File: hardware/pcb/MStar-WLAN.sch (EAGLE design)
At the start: 39 parts, among them J1 6P6C, J3 ZX62R-B-5P(30), Q1 VP2106, Q2 2N3904

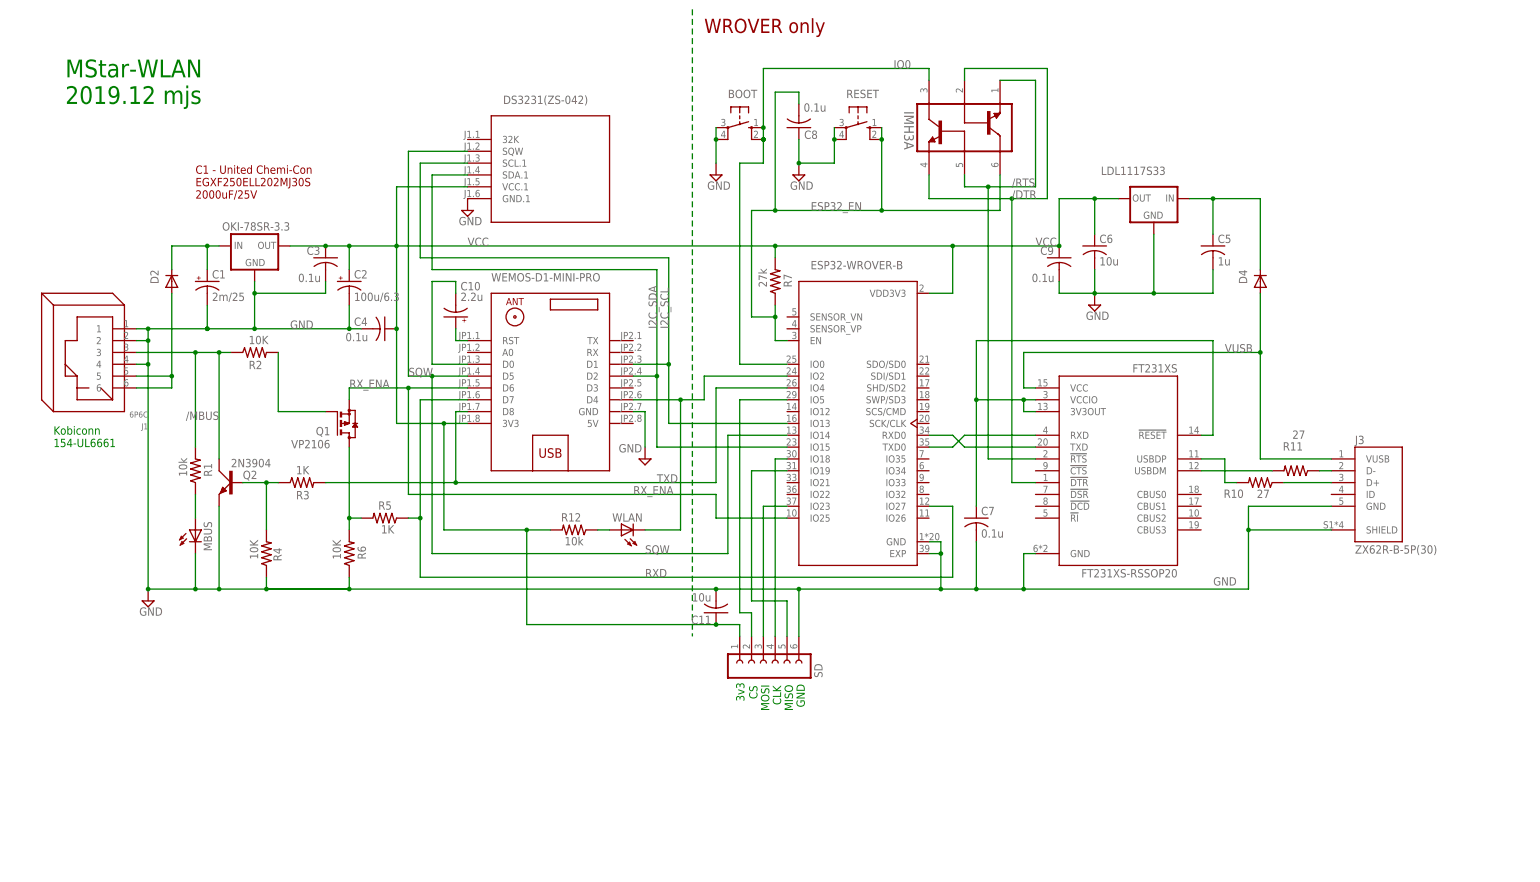
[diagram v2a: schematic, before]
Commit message: bug fixes. SD Card support. New PCB.
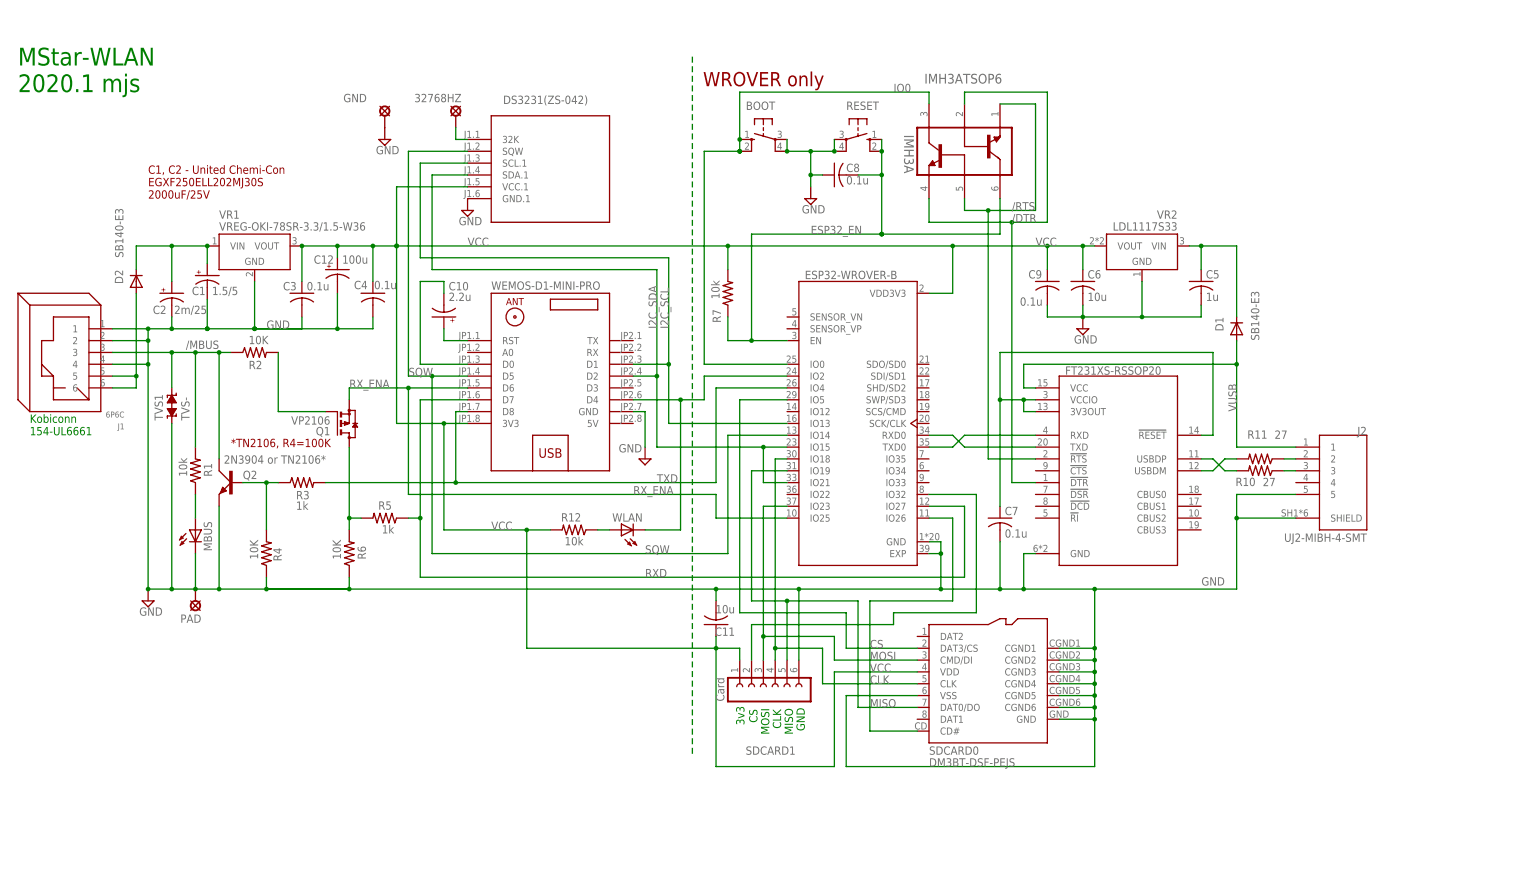
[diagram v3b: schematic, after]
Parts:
- removed D4: (no value), diode:DIODE-D-5
- removed J3: ZX62R-B-5P(30), MyLibrary:ZX62R-B-5P(30)
- removed LDL1117S33: LM1117MP-3.3, MyLibrary:LM1117MP-3.3
- removed OKI-78SR-3.3: (no value), v-reg:78MXXS
- removed SD: (no value), con-lsta:FE06-1
- added 32768HZ, GND: MCS10B, MStar-WLAN:MCS10B
- added C12: 100u, MStar-WLAN:CPOL-USE2.5-6
- added D1: SB140-E3, MStar-WLAN:DIODE-
- added J2: UJ2-MIBH-4-SMT, MStar-WLAN:UJ2-MIBH-4-SMT
- added PAD: LSP10, MStar-WLAN:LSP10
- added SDCARD0: DM3BT-DSF-PEJS, MStar-WLAN:DM3BT-DSF-PEJS
- added SDCARD1: Card, MStar-WLAN:FE06-1
- added TVS1: TVS-, MStar-WLAN:TVS-
- added VR1: VREG-OKI-78SR-3.3/1.5-W36, MStar-WLAN:VREG-OKI-78SR-3.3/1.5-W36
- added VR2: LDL1117S33, MStar-WLAN:VREG-TS1117CW-3V3
- BOOT, RESET: device switch-omron:10-XX -> MStar-WLAN:10-XX
- C1: value 2m/25 -> 1.5/5; device rcl:CPOL-USE5-10.5 -> MStar-WLAN:CPOL-USE5-4
- C10: device rcl:CPOL-USE2.5-5 -> MStar-WLAN:CPOL-USE2.5-5
- C11, C5, C6: device rcl:C-USC1206 -> MStar-WLAN:C-USC1206
- C2: value 100u/6.3 -> 2m/25; device rcl:CPOL-USE2.5-6 -> MStar-WLAN:CPOL-USE5-4
- C3, C4, C7, C8, C9: device rcl:C-US025-024X044 -> MStar-WLAN:C-US025-024X044
- D2: value (none) -> SB140-E3; device diode:DIODE-D-5 -> MStar-WLAN:DIODE-DO41-7.6
- DS3231(ZS-042): device MyLibrary:RTC-DS3231-AT24C32-6 -> MStar-WLAN:RTC-DS3231-AT24C32-6
- ESP32-WROVER-B: device MyLibrary:ESP32-WROVER-I -> MStar-WLAN:ESP32-WROVER-I
- FT231XS: device MyLibrary:FT231XS-RSSOP20 -> MStar-WLAN:FT231XS-RSSOP20
- IMH3A: device MyLibrary:IMH3ATSOP6 -> MStar-WLAN:IMH3ATSOP6
- J1: device con-rj:RJ12 -> MStar-WLAN:RJ12
- MBUS, WLAN: device adafruit:LED3MM -> MStar-WLAN:LED3MM
- Q1: device MyLibrary:VP2106 -> MStar-WLAN:VP2106
- Q2: value 2N3904 -> 2N3904 or TN2106*; device transistor-small-signal:2N3904 -> MStar-WLAN:2N3904"
- R1, R10, R11, R12, R2, R4, R6: device rcl:R-US_0207/2V -> MStar-WLAN:R-US_
- R3, R5: value 1K -> 1k; device rcl:R-US_0207/2V -> MStar-WLAN:R-US_
- R7: value 27k -> 10k; device rcl:R-US_0207/2V -> MStar-WLAN:R-US_
- U$1: device MyLibrary:WEMOS-D1-MINI-PRO -> MStar-WLAN:WEMOS-D1-MINI-PRO
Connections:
- net N$19 renamed WLAN_LED
- net N$4 renamed WEMOS_RST
- net N$5 renamed TXD0
- net N$6 renamed RXD0
- net N$7 renamed SELF_RESET
- removed net N$16: ESP32-WROVER-B.IO5, SD.2
- removed net N$20: ESP32-WROVER-B.IO18, SD.4
- removed net N$22: ESP32-WROVER-B.IO23, SD.3
- removed net N$8: ESP32-WROVER-B.IO19, SD.5
- new net CLK: ESP32-WROVER-B.IO18, SDCARD0.CLK, SDCARD1.4
- new net CS: ESP32-WROVER-B.IO5, SDCARD0.DAT3/CS
- new net MISO: ESP32-WROVER-B.IO19, SDCARD0.DAT0/DO, SDCARD1.5
- new net MOSI: ESP32-WROVER-B.IO23, SDCARD0.CMD/DI, SDCARD1.3
- new net N$4: ESP32-WROVER-B.IO26, SDCARD0.CD#
- new net N$5: 32768HZ.MP, DS3231(ZS-042).32K
- new net N$7: ESP32-WROVER-B.IO32, SDCARD1.2
- net /MBUS: now also TVS1.2
- net GND: now also C12.-, GND.MP, J2.5, J2.SHIELD, PAD.MP, SDCARD0.CGND1, SDCARD0.CGND2, SDCARD0.CGND3, SDCARD0.CGND4, SDCARD0.CGND5, SDCARD0.CGND6, SDCARD0.GND, SDCARD0.VSS, SDCARD1.6, TVS1.1, VR1.GND, VR2.GND; no longer J3.GND, J3.SHIELD, LDL1117S33.GND, OKI-78SR-3.3.GND, SD.6
- net I2C_SDA: now also ESP32-WROVER-B.IO21
- net N$10: now also J2.2; no longer J3.D-
- net N$17: now also D1.C, VR2.VIN; no longer D4.C, LDL1117S33.IN
- net N$9: now also J2.3; no longer J3.D+
- net RAW12: now also C2.+, VR1.VIN; no longer OKI-78SR-3.3.IN
- net VCC: now also C12.+, SDCARD0.VDD, SDCARD1.1, VR1.VOUT, VR2.VOUT; no longer C2.+, LDL1117S33.OUT, OKI-78SR-3.3.OUT, SD.1
- net VUSB: now also D1.A, J2.1; no longer D4.A, J3.VUSB
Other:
- note added: "*TN2106, R4=100K"
- note added: "C1, C2 - United Chemi-Con EGXF250ELL202MJ30S 2000uF/25V"
- note added: "MStar-WLAN 2020.1 mjs"
- note removed: "C1 - United Chemi-Con EGXF250ELL202MJ30S 2000uF/25V"
- note removed: "MStar-WLAN 2019.12 mjs"
- moved on the sheet: BOOT, D2, IMH3A, J1, R10, R11, R7, RESET

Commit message: ESP32. Logging. Dynamic status update. More.
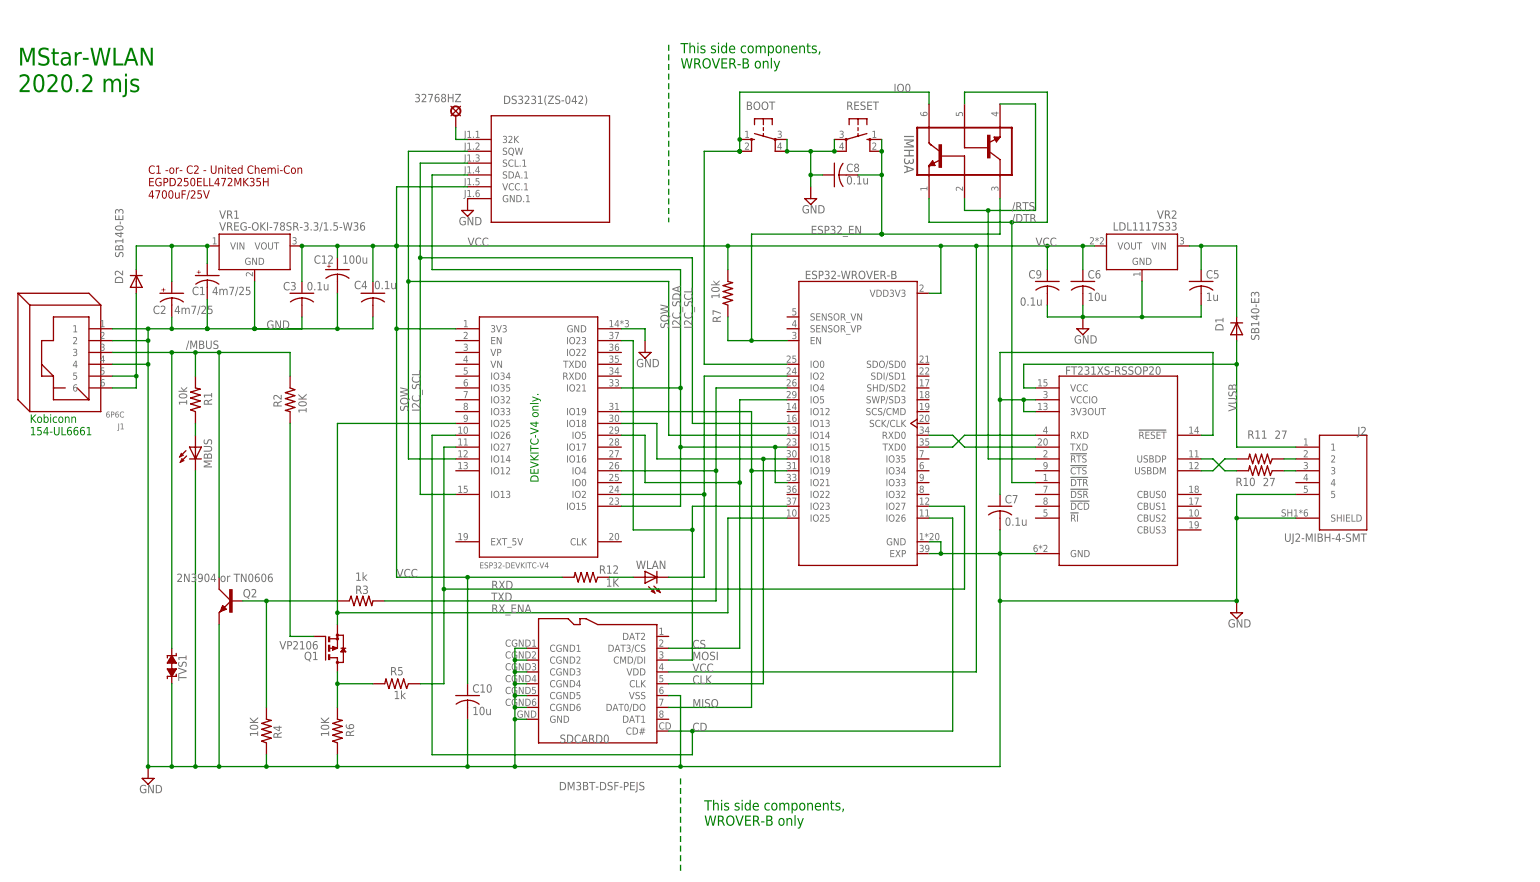
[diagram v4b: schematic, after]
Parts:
- removed C11: 10u, MStar-WLAN:C-USC1206
- removed GND: MCS10B, MStar-WLAN:MCS10B
- removed PAD: LSP10, MStar-WLAN:LSP10
- removed SDCARD1: Card, MStar-WLAN:FE06-1
- C1: value 1.5/5 -> 4m7/25
- C10: value 2.2u -> 10u; device MStar-WLAN:CPOL-USE2.5-5 -> MStar-WLAN:C-USC1206
- C2: value 2m/25 -> 4m7/25
- Q2: value 2N3904 or TN2106* -> 2N3904 or TN0606
- R12: value 10k -> 1K
- U$1: value WEMOS-D1-MINI-PRO -> ESP32-DEVKITC-V4-NOSD; device MStar-WLAN:WEMOS-D1-MINI-PRO -> MStar-WLAN:ESP32-DEVKITC-V4-NOSD
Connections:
- removed net N$4: ESP32-WROVER-B.IO26, SDCARD0.CD#
- removed net N$7: ESP32-WROVER-B.IO32, SDCARD1.2
- removed net SELF_RESET: C10.-, U$1.D0
- removed net WEMOS_RST: C10.+, U$1.RST
- new net CD: ESP32-WROVER-B.IO26, SDCARD0.CD#, U$1.IO26
- net /DTR: now also IMH3A.Q1E, IMH3A.Q2B; no longer IMH3A.Q1B, IMH3A.Q2E
- net /RTS: now also IMH3A.Q1B, IMH3A.Q2E; no longer IMH3A.Q1E, IMH3A.Q2B
- net CLK: now also U$1.IO18; no longer SDCARD1.4
- net CS: now also U$1.IO5
- net ESP32_EN: now also IMH3A.Q2C; no longer IMH3A.Q1C
- net GND: now also C10.2; no longer C11.2, GND.MP, PAD.MP, SDCARD1.6
- net I2C_SCL: now also U$1.IO13; no longer U$1.D1
- net I2C_SDA: now also U$1.IO15, U$1.IO21; no longer U$1.D2
- net IO0: now also IMH3A.Q1C; no longer IMH3A.Q2C
- net MISO: now also U$1.IO19; no longer SDCARD1.5
- net MOSI: now also U$1.IO23; no longer SDCARD1.3
- net RXD: now also U$1.IO27; no longer U$1.D7
- net RX_ENA: now also U$1.IO25; no longer U$1.D6
- net SQW: now also U$1.IO14; no longer U$1.D5
- net TXD: now also U$1.IO4; no longer U$1.D8
- net VCC: now also C10.1; no longer C11.1, SDCARD1.1
- net WLAN_LED: now also U$1.IO2; no longer U$1.D4
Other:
- note added: "C1 -or- C2 - United Chemi-Con EGPD250ELL472MK35H 4700uF/25V"
- note added: "DEVKITC-V4 only."
- note added: "MStar-WLAN 2020.2 mjs"
- note added: "This side components, WROVER-B only"
- note removed: "*TN2106, R4=100K"
- note removed: "3v3"
- note removed: "C1, C2 - United Chemi-Con EGXF250ELL202MJ30S 2000uF/25V"
- note removed: "CLK"
- note removed: "CS"
- note removed: "GND"
- note removed: "MISO"
- note removed: "MOSI"
- note removed: "MStar-WLAN 2020.1 mjs"
- note removed: "WROVER only"
- moved on the sheet: C7, IMH3A, MBUS, Q1, Q2, R1, R12, R2, R3, R4, R5, R6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

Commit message: Logging, hardware change to USB C
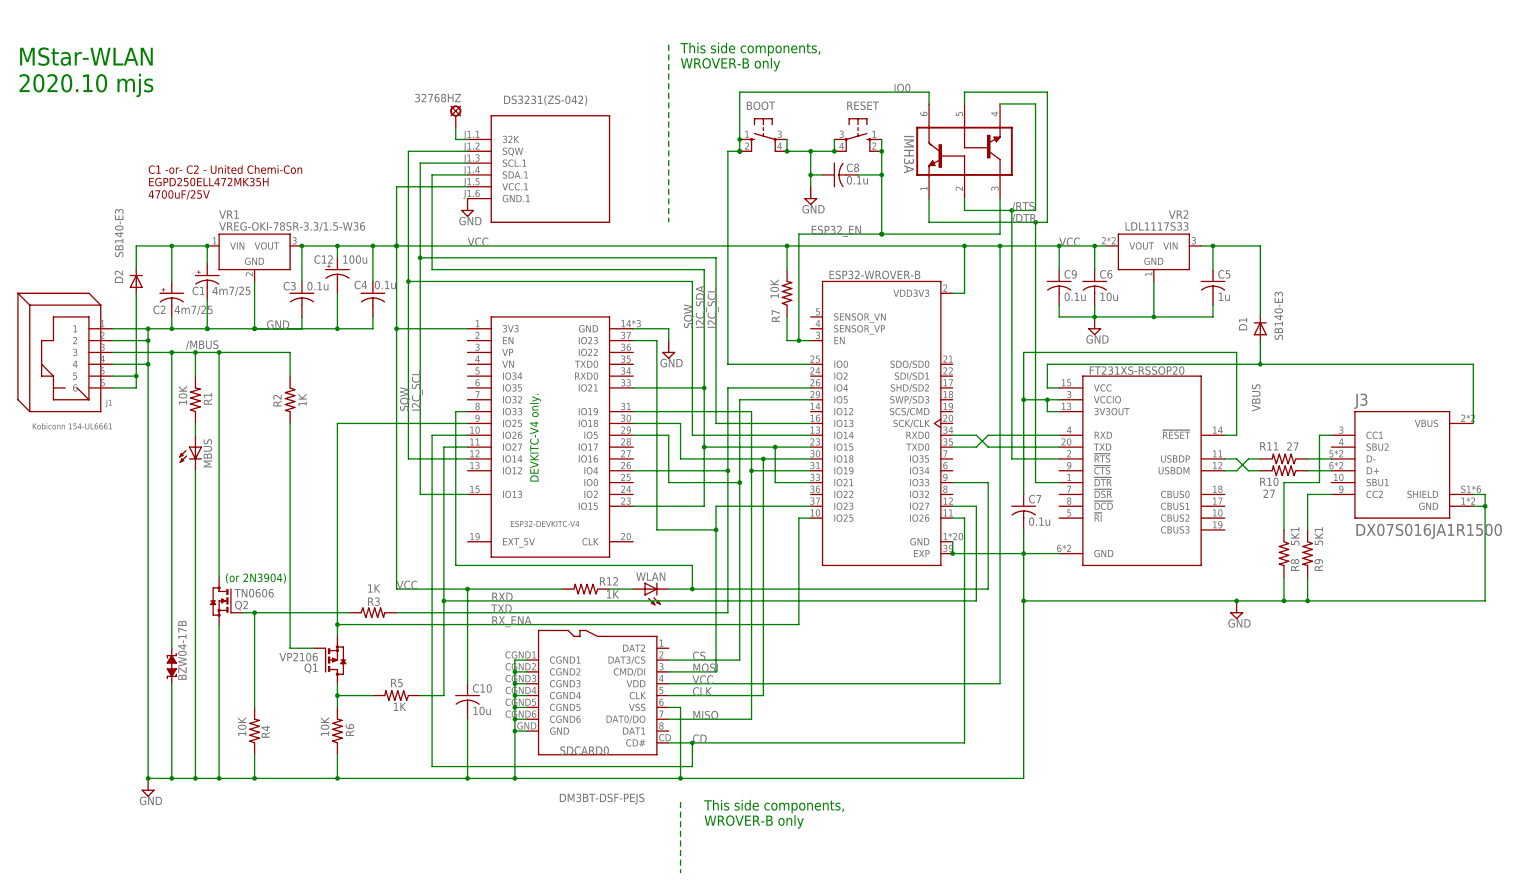
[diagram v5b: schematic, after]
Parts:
- removed J2: UJ2-MIBH-4-SMT, MStar-WLAN:UJ2-MIBH-4-SMT
- added J3: DX07S016JA1R1500, MStar-WLAN:DX07S016JA1R1500
- added R8, R9: 5K1, MStar-WLAN:R-US_
- C12: device MStar-WLAN:CPOL-USE2.5-6 -> rcl:CPOL-USE5-8.5
- D1: device MStar-WLAN:DIODE- -> MStar-WLAN:DIODE-DO41-7.6
- J1: value 6P6C -> Kobiconn 154-UL6661
- Q2: value 2N3904 or TN0606 -> TN0606; device MStar-WLAN:2N3904" -> MStar-WLAN:TN0606
- R1, R7: value 10k -> 10K
- R2: value 10K -> 1K
- R3, R5: value 1k -> 1K
- renumbered TVS1 to BZW04-17B
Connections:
- net N$11 renamed USBDP
- net N$13 renamed USBDM
- removed net N$10: J2.2, R11.1
- removed net N$9: J2.3, R10.1
- removed net VUSB: D1.A, FT231XS.VCC, J2.1
- new net N$6: J3.CC2, R9.1
- new net N$7: J3.CC1, R8.1
- new net USBD+: J3.D+, R10.1
- new net USBD-: J3.D-, R11.1
- new net VBUS: D1.A, FT231XS.VCC, J3.VBUS
- net /MBUS: now also Q2.D; no longer Q2.C
- net GND: now also J3.GND, J3.SHIELD, Q2.S, R8.2, R9.2; no longer J2.5, J2.SHIELD, Q2.E
- net N$2: now also Q2.G; no longer Q2.B
- net WLAN_LED: now also ESP32-WROVER-B.IO33, U$1.IO33; no longer ESP32-WROVER-B.IO2, U$1.IO2
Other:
- note added: "(or 2N3904)"
- note added: "MStar-WLAN 2020.10 mjs"
- note removed: "Kobiconn 154-UL6661"
- note removed: "MStar-WLAN 2020.2 mjs"
- moved on the sheet: C5, C6, C7, C9, D1, ESP32-WROVER-B, Q1, R10, R11, R12, R3, R4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
